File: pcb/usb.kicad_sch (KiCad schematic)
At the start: 7 parts, among them J1 12401598E4#2A, U2 USBLC6-2P6

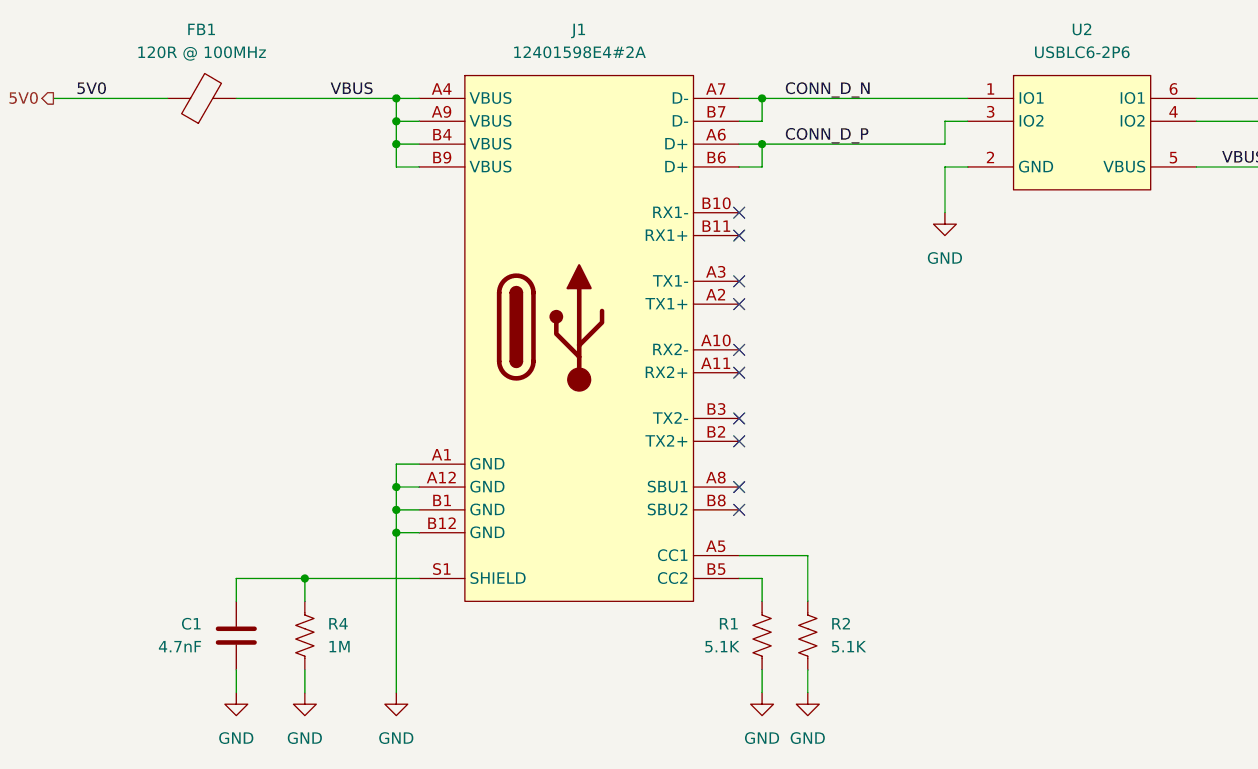
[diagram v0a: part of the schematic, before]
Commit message: kb matrix complete, stm32 wiring done
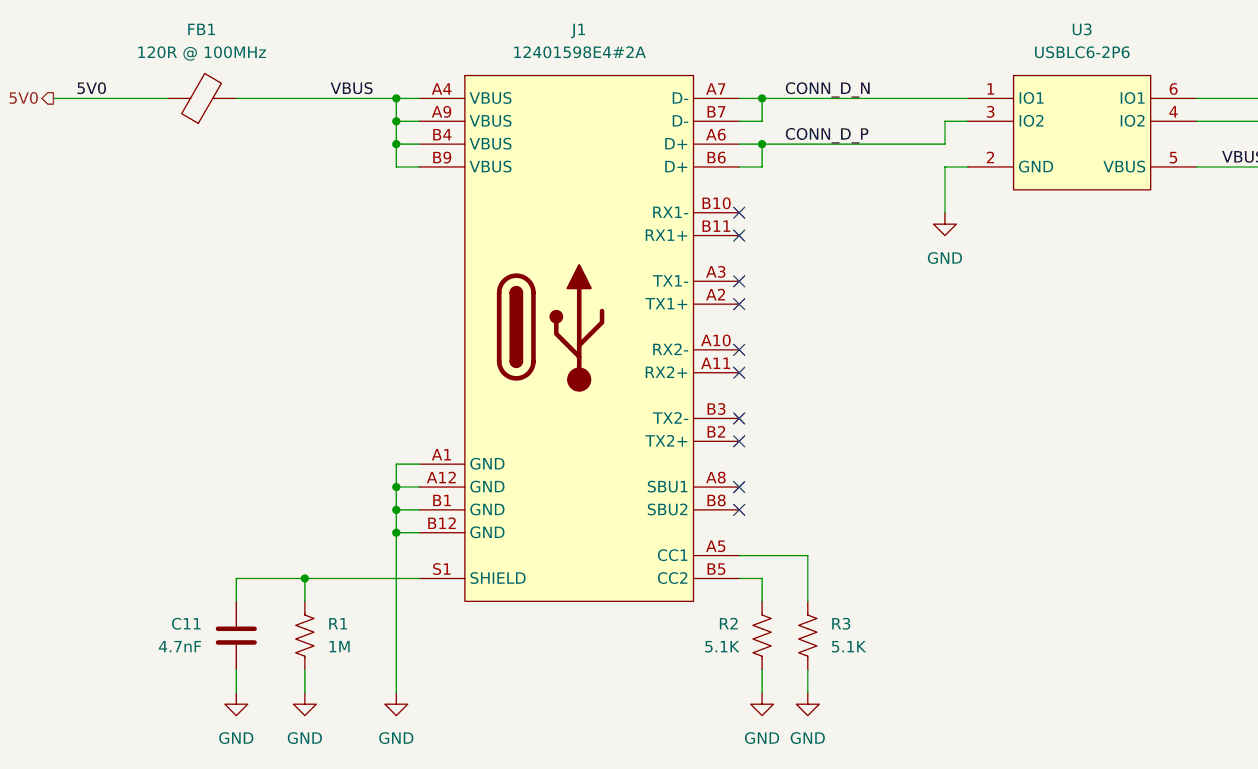
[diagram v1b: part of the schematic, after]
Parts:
- renumbered C1 to C11, R4 to R1, R1 to R2, R2 to R3, U2 to U3
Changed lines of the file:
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@@
 		(dnp no)
 		(fields_autoplaced yes)
-		(property "Reference" "#PWR05"
+		(property "Reference" "#PWR014"
 			(at 96.52 140.97 0)
 			(effects
@@
 			(project "alana-kb"
 				(path "/14664179-4b45-478a-8e33-e1eaac937d3d/2255f5ec-0f5b-4119-872e-88e5f6171d9e"
-					(reference "#PWR05")
+					(reference "#PWR014")
 					(unit 1)
 				)
@@
 		(on_board yes)
 		(dnp no)
-		(property "Reference" "R2"
+		(property "Reference" "R3"
 			(at 162.56 127 0)
 			(effects
@@
 			(project "alana-kb"
 				(path "/14664179-4b45-478a-8e33-e1eaac937d3d/2255f5ec-0f5b-4119-872e-88e5f6171d9e"
-					(reference "R2")
+					(reference "R3")
 					(unit 1)
 				)
@@
 		(on_board yes)
 		(dnp no)
-		(property "Reference" "R4"
+		(property "Reference" "R1"
 			(at 106.68 126.9999 0)
 			(effects
@@
 			(project "alana-kb"
 				(path "/14664179-4b45-478a-8e33-e1eaac937d3d/2255f5ec-0f5b-4119-872e-88e5f6171d9e"
-					(reference "R4")
+					(reference "R1")
 					(unit 1)
 				)
@@
 		(dnp no)
 		(fields_autoplaced yes)
-		(property "Reference" "#PWR02"
+		(property "Reference" "#PWR013"
 			(at 175.26 87.63 0)
 			(effects
@@
 			(project "alana-kb"
 				(path "/14664179-4b45-478a-8e33-e1eaac937d3d/2255f5ec-0f5b-4119-872e-88e5f6171d9e"
-					(reference "#PWR02")
+					(reference "#PWR013")
 					(unit 1)
 				)
@@
 		(dnp no)
 		(fields_autoplaced yes)
-		(property "Reference" "U2"
+		(property "Reference" "U3"
 			(at 190.5 60.96 0)
 			(effects
@@
 			(project "alana-kb"
 				(path "/14664179-4b45-478a-8e33-e1eaac937d3d/2255f5ec-0f5b-4119-872e-88e5f6171d9e"
-					(reference "U2")
+					(reference "U3")
 					(unit 1)
 				)
@@
 		(dnp no)
 		(fields_autoplaced yes)
-		(property "Reference" "#PWR01"
+		(property "Reference" "#PWR016"
 			(at 114.3 140.97 0)
 			(effects
@@
 			(project "alana-kb"
 				(path "/14664179-4b45-478a-8e33-e1eaac937d3d/2255f5ec-0f5b-4119-872e-88e5f6171d9e"
-					(reference "#PWR01")
+					(reference "#PWR016")
 					(unit 1)
 				)
@@
 		(on_board yes)
 		(dnp no)
-		(property "Reference" "C1"
+		(property "Reference" "C11"
 			(at 92.71 126.9999 0)
 			(effects
@@
 			(project "alana-kb"
 				(path "/14664179-4b45-478a-8e33-e1eaac937d3d/2255f5ec-0f5b-4119-872e-88e5f6171d9e"
-					(reference "C1")
+					(reference "C11")
 					(unit 1)
 				)
@@
 		(dnp no)
 		(fields_autoplaced yes)
-		(property "Reference" "#PWR06"
+		(property "Reference" "#PWR015"
 			(at 104.14 140.97 0)
 			(effects
@@
 			(project "alana-kb"
 				(path "/14664179-4b45-478a-8e33-e1eaac937d3d/2255f5ec-0f5b-4119-872e-88e5f6171d9e"
-					(reference "#PWR06")
+					(reference "#PWR015")
 					(unit 1)
 				)
@@
 		(dnp no)
 		(fields_autoplaced yes)
-		(property "Reference" "#PWR04"
+		(property "Reference" "#PWR017"
 			(at 154.94 140.97 0)
 			(effects
@@
 			(project "alana-kb"
 				(path "/14664179-4b45-478a-8e33-e1eaac937d3d/2255f5ec-0f5b-4119-872e-88e5f6171d9e"
-					(reference "#PWR04")
+					(reference "#PWR017")
 					(unit 1)
 				)
@@
 		(dnp no)
 		(fields_autoplaced yes)
-		(property "Reference" "#PWR03"
+		(property "Reference" "#PWR018"
 			(at 160.02 140.97 0)
 			(effects
@@
 			(project "alana-kb"
 				(path "/14664179-4b45-478a-8e33-e1eaac937d3d/2255f5ec-0f5b-4119-872e-88e5f6171d9e"
-					(reference "#PWR03")
+					(reference "#PWR018")
 					(unit 1)
 				)
@@
 		(on_board yes)
 		(dnp no)
-		(property "Reference" "R1"
+		(property "Reference" "R2"
 			(at 152.4 127 0)
 			(effects
@@
 			(project "alana-kb"
 				(path "/14664179-4b45-478a-8e33-e1eaac937d3d/2255f5ec-0f5b-4119-872e-88e5f6171d9e"
-					(reference "R1")
-					(unit 1)
-				)
+					(reference "R2")
+					(unit 1)
+				)

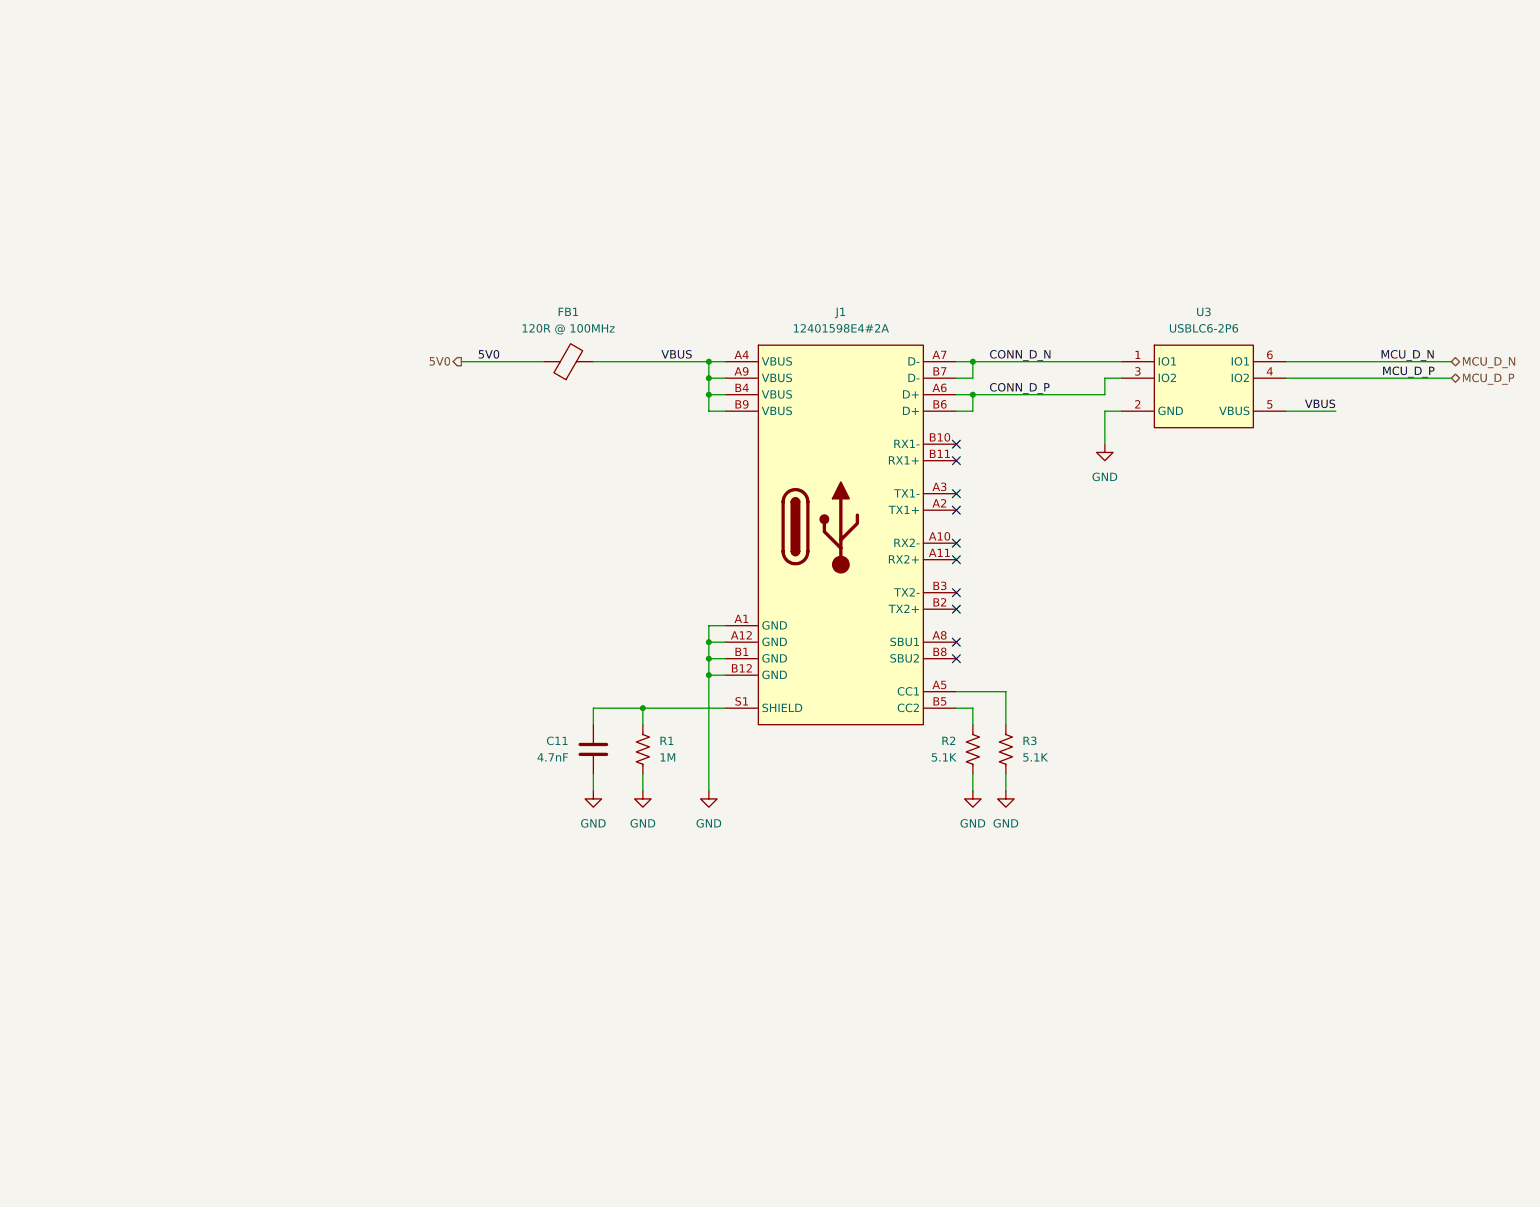
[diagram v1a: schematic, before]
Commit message: replaced usb c with molex for udb
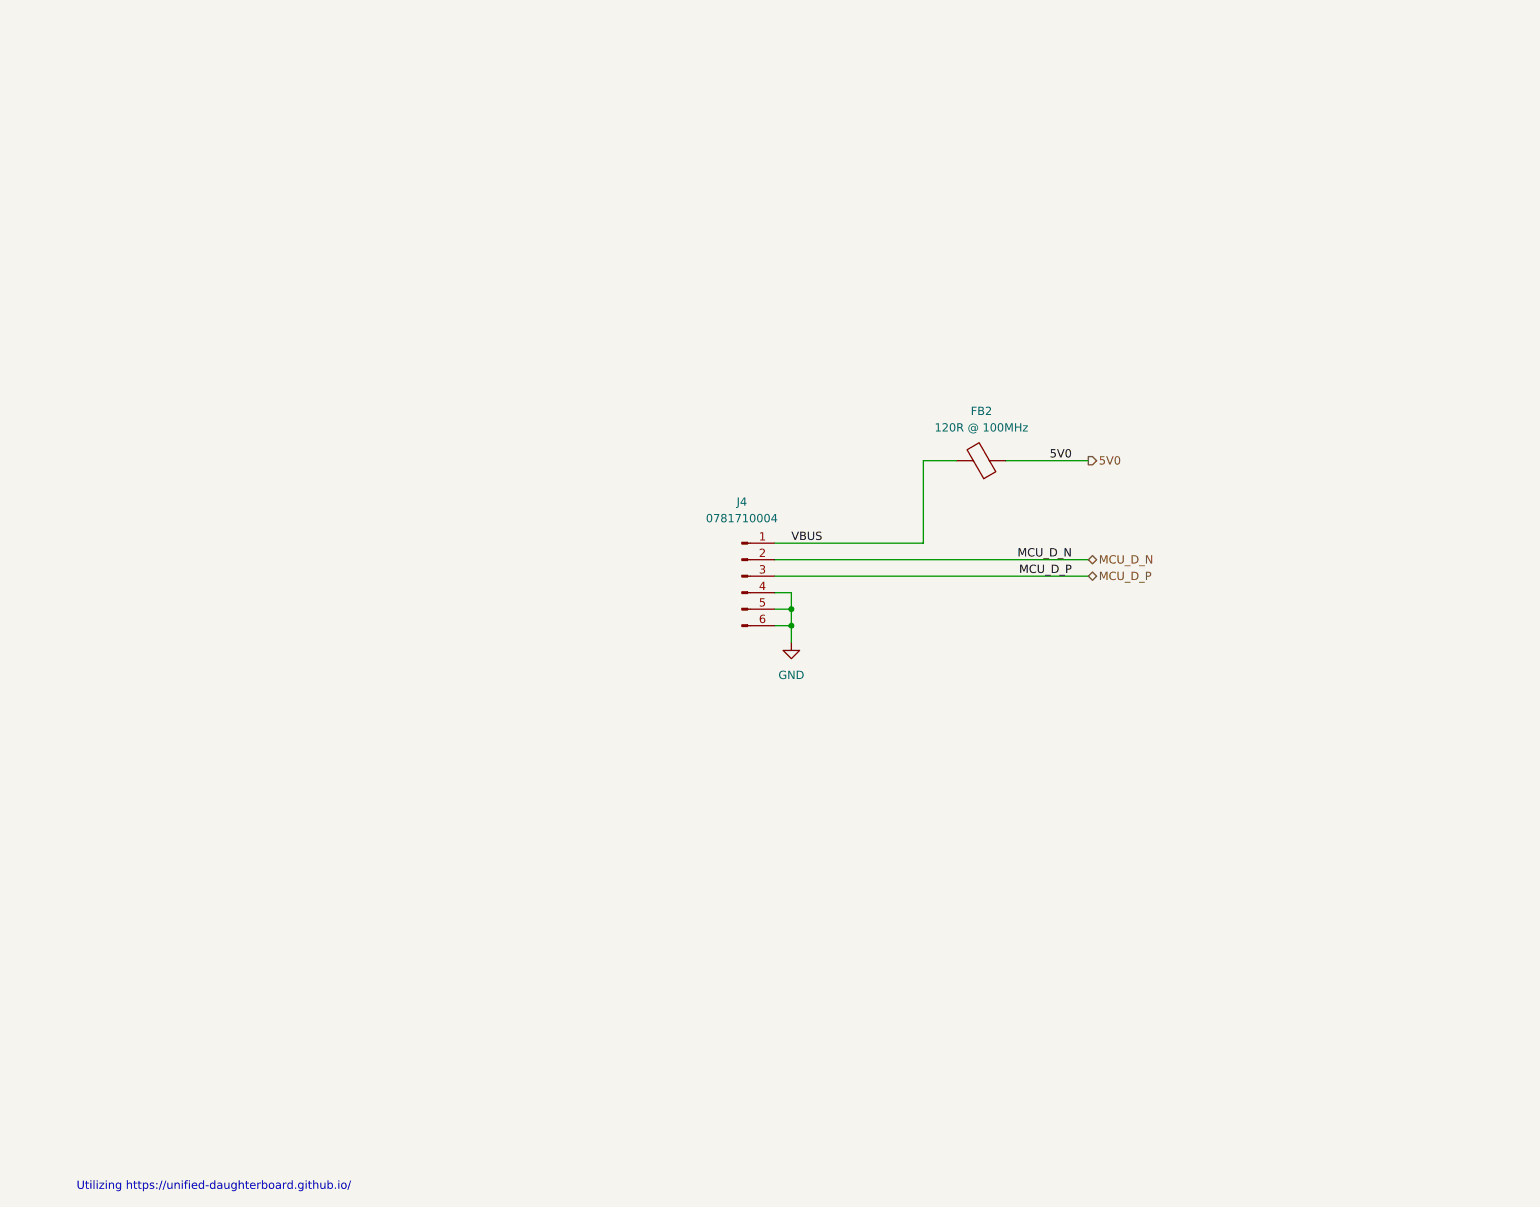
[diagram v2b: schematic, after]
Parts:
- removed C11: 4.7nF, Capacitor_SMD:C_0402_1005Metric, symbol Device:C
- removed FB1: 120R @ 100MHz, Inductor_SMD:L_0805_2012Metric, symbol Device:FerriteBead
- removed J1: 12401598E4#2A, library:AMPHENOL_12401598E4_2A, symbol library:12401598E4#2A
- removed R1: 1M, Resistor_SMD:R_0402_1005Metric, symbol Device:R_US
- removed R2, R3: 5.1K, Resistor_SMD:R_0402_1005Metric, symbol Device:R_US
- removed U3: USBLC6-2P6, Package_TO_SOT_SMD:SOT-666, symbol library:USBLC6-2P6
- added FB2: 120R @ 100MHz, Inductor_SMD:L_0805_2012Metric, symbol Device:FerriteBead
- added J4: 0781710004, library:CONN_781710000-SD_04_MOL, symbol Connector:Conn_01x06_Pin
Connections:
- net 5V0: now also FB2.1
- net GND: now also J4.4 (Pin_4), J4.5 (Pin_5), J4.6 (Pin_6)
- net MCU_D_N: now also J4.2 (Pin_2)
- net MCU_D_P: now also J4.3 (Pin_3)
- net VBUS: now also FB2.2, J4.1 (Pin_1)
- no-connect marks 10 -> 0
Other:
- note added: "Utilizing https://unified-daughterboard.github.io/"

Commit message: reroute matrix
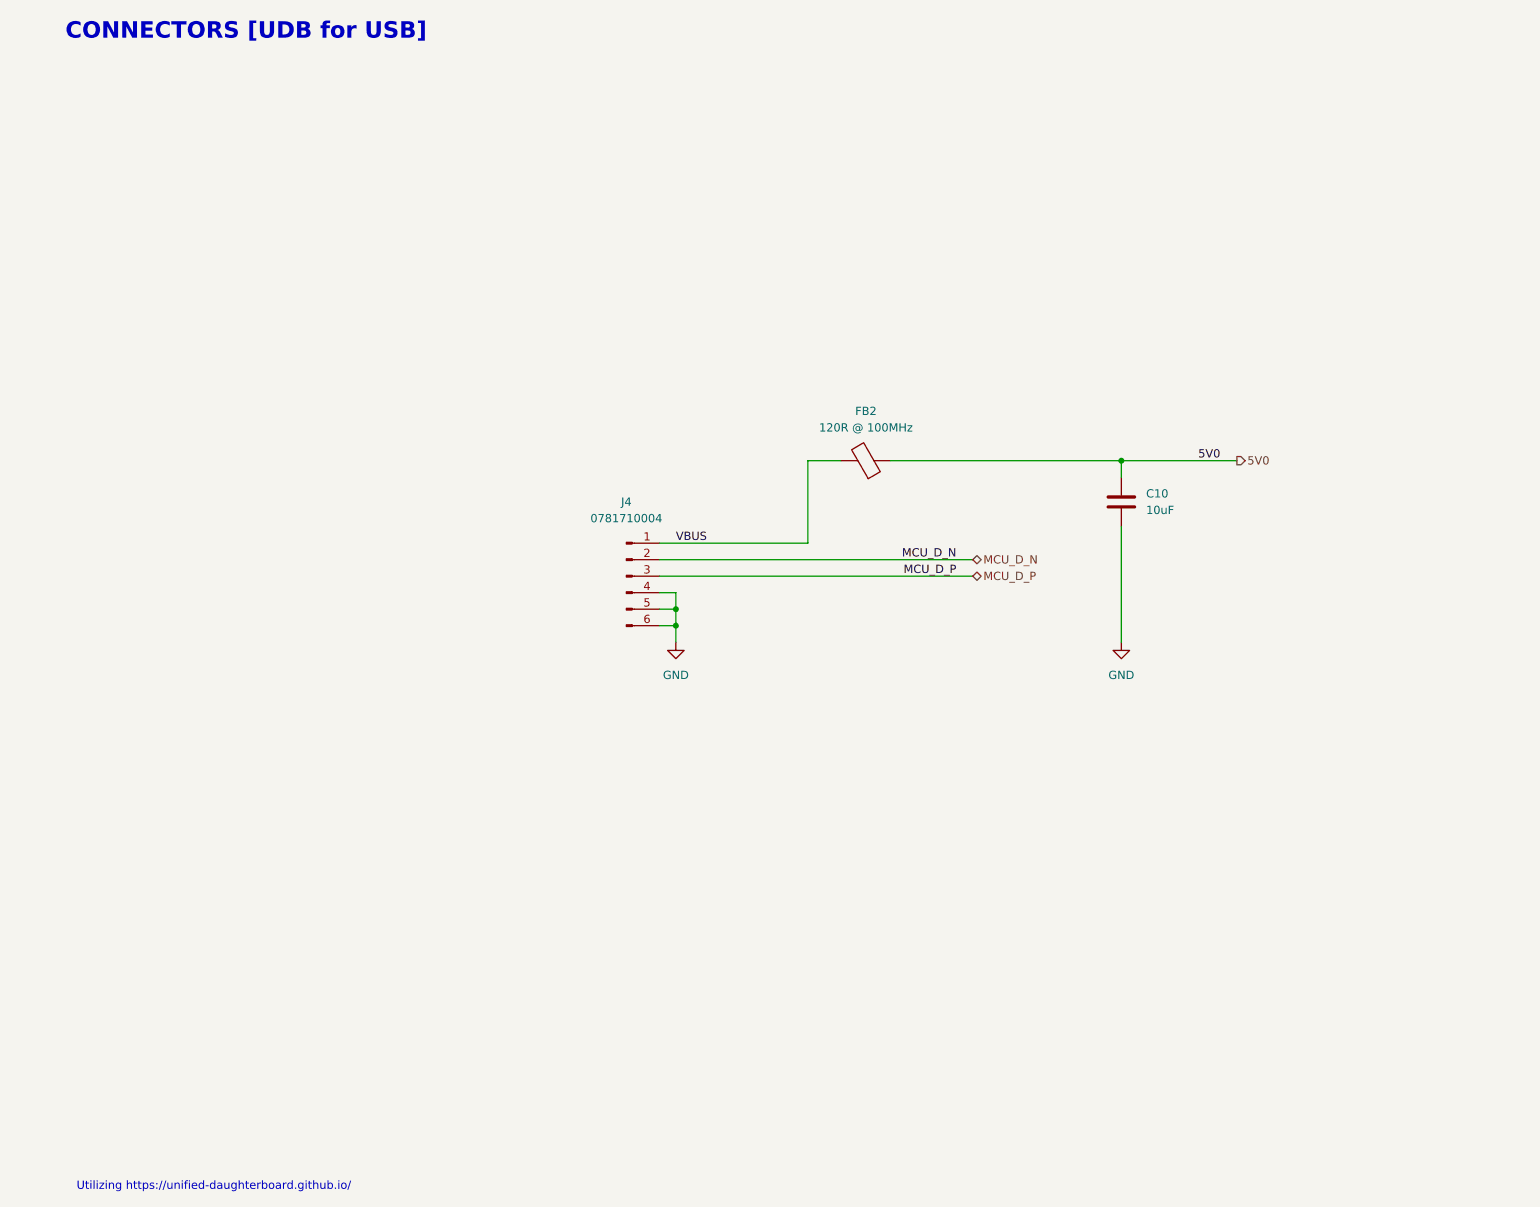
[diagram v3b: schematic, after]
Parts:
- added C10: 10uF, Capacitor_SMD:C_0805_2012Metric, symbol Device:C
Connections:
- net 5V0: now also C10.1
- net GND: now also C10.2
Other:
- note added: "CONNECTORS [UDB for USB]"
- company: (none) -> ASE, ASW, AMB
- title: (none) -> ALANA-KB PCB
- moved on the sheet: FB2, J4

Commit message: bom fb part, complete
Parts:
- FB2: Manufacturer Product Number BLM18PG121SN1D -> BLM21PG121SN1D
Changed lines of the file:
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@@
 			)
 		)
-		(property "Description" "FERRITE BEAD 120 OHM 0603 1LN"
+		(property "Description" "FERRITE BEAD 120 OHM 0805 1LN"
 			(at 138.43 83.82 0)
 			(effects
@@
 			)
 		)
-		(property "Manufacturer Product Number" "BLM18PG121SN1D"
+		(property "Manufacturer Product Number" "BLM21PG121SN1D"
 			(at 138.43 83.82 90)
 			(effects
